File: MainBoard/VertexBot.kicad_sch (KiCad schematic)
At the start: 52 parts, among them J1 Battery, J2 I2C Extension, J4 Left Motor, J5 Right Motor, J6 Led Strip, Q1 BSS138, Q2 BSS138, Q3 BSS138, SW1 SW_SPST, U1 DRV8830DGQR, U10 MAX4466 (LEFT), U11 MAX4466 (RIGHT), U12 ESP32-S3-CAM-B, U13 ESP32-S3-CAM-A, U14 MAX98357A, U2 DRV8830DGQR, U3 S13V30F5, U5 INMP441, U6 0.96 INCH OLED, U7 DRV5033AJxLPG, U8 DRV5033AJxLPG, U9 MPU 6050

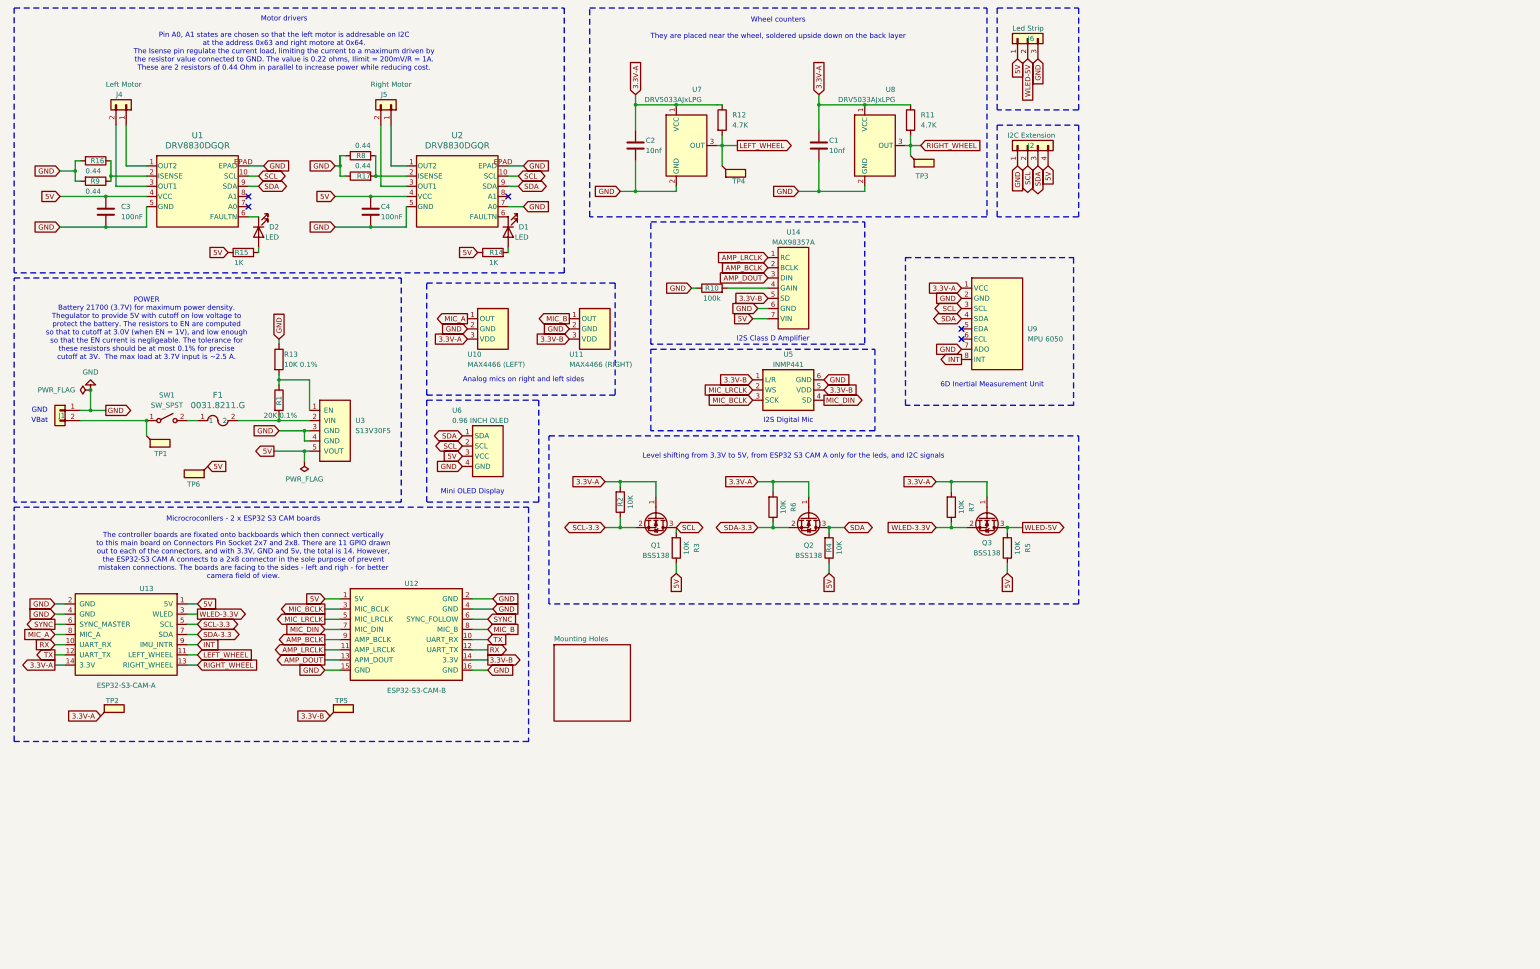
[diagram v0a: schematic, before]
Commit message: Adjust DRV8830DGQR to allow thermal pad connect to GND Adjust some of the modules courtyard Fix mounting holes symbols to have connection
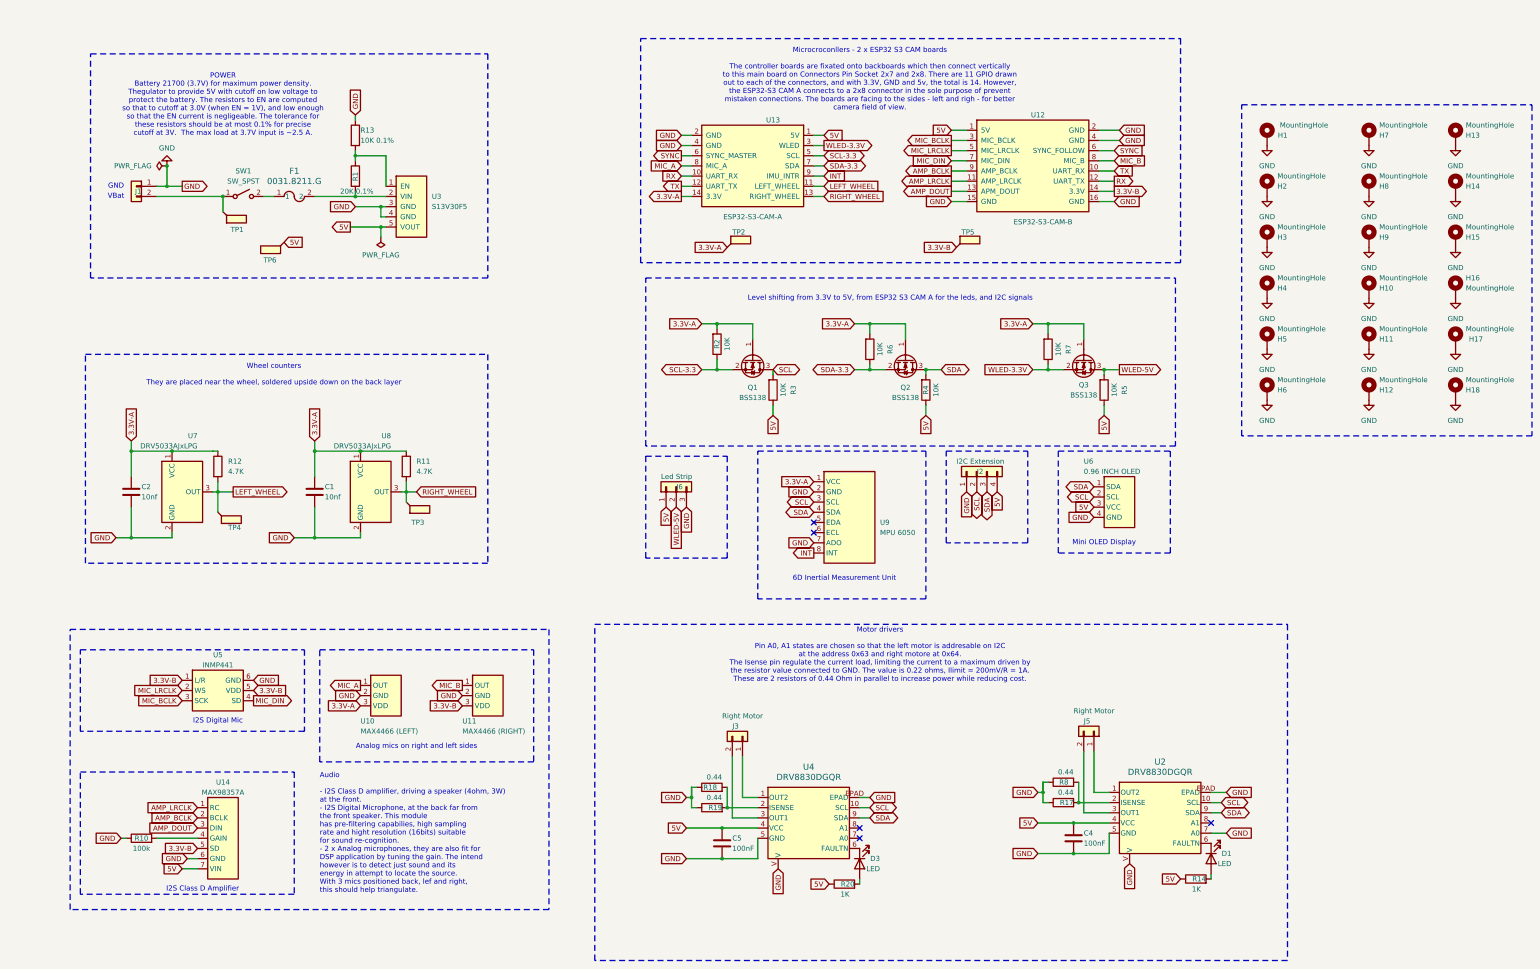
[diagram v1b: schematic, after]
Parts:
- removed C3: 100nF, Capacitor_SMD:C_0603_1608Metric, symbol Device:C
- removed D2: LED, LED_SMD:LED_0805_2012Metric, symbol Device:LED
- removed J4: Left Motor, Connector_JST:JST_PH_S2B-PH-K_1x02_P2.00mm_Horizontal, symbol Connector_Generic:Conn_01x02
- removed R15: 1K, Resistor_SMD:R_0603_1608Metric, symbol Device:R
- removed R16, R9: 0.44, Resistor_SMD:R_0603_1608Metric, symbol Device:R
- removed U1: DRV8830DGQR, Vertex_Bot:DGQ10_2P18X1P72, symbol DRV8830:DRV8830DGQR
- added C5: 100nF, Capacitor_SMD:C_0603_1608Metric, symbol Device:C
- added D3: LED, LED_SMD:LED_0805_2012Metric, symbol Device:LED
- added H1, H10, H11, H12, H13, H14, H15, H16, H17, H18, H2, H3, H4, H5, H6, H7, H8, H9: MountingHole, MountingHole:MountingHole_3.5mm_Pad, symbol Mechanical:MountingHole_Pad
- added J3: Right Motor, Connector_JST:JST_PH_S2B-PH-K_1x02_P2.00mm_Horizontal, symbol Connector_Generic:Conn_01x02
- added R18: 0.44, Resistor_SMD:R_0603_1608Metric, symbol Device:R
- added R19: 0.44, Resistor_SMD:R_1206_3216Metric, symbol Device:R
- added R20: 1K, Resistor_SMD:R_0603_1608Metric, symbol Device:R
- added U4: DRV8830DGQR, Vertex_Bot:DGQ10_2P18X1P72, symbol DRV8830:DRV8830DGQR
- J2: footprint Connector_JST:JST_XH_S3B-XH-A-1_1x03_P2.50mm_Horizontal -> Connector_PinHeader_2.54mm:PinHeader_1x04_P2.54mm_Vertical
- R17: footprint Resistor_SMD:R_0603_1608Metric -> Resistor_SMD:R_1206_3216Metric
- U7, U8: footprint Package_TO_SOT_THT:TO-92Flat -> Package_TO_SOT_THT:TO-92_Inline
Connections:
- net 5V: now also C5.1, R20.1, U4.4 (VCC)
- net GND: now also U2.V, C5.2, H1.1, H10.1, H11.1, H12.1, H13.1, H14.1, H15.1, H16.1, H17.1, H18.1, H2.1, H3.1, H4.1, H5.1, H6.1, H7.1, H8.1, H9.1, R18.1, R19.1, U4.5 (GND), U4.EPAD, U4.V
- net SCL: now also U4.10 (SCL)
- net SDA: now also U4.9 (SDA)
- new net: D3.2 (A), R20.2
- new net: J3.1 (Pin_1), U4.1 (OUT2)
- new net: R18.2, R19.2, U4.2 (ISENSE)
- new net: J3.2 (Pin_2), U4.3 (OUT1)
- new net: D3.1 (K), U4.6 (FAULTN)
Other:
- removed sheet Mounting Holes
- note added: "Audio - I2S Class D amplifier, driving a speaker (4ohm, 3W) at the front. - I2S Digital Microphone, at the back far from the front speaker. This module has pre-filtering capabilies, high sampling rate and hight resolution (16bits) suitable for sound re-cognition. - 2 x Analog microphones, they are also fit for DSP application by tuning the gain. The intend however is to detect just sound and its 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"
- note added: "Level shifting from 3.3V to 5V, from ESP32 S3 CAM A for the leds, and I2C signals"
- note removed: "Level shifting from 3.3V to 5V, from ESP32 S3 CAM A only for the leds, and I2C signals"
- moved on the sheet: C1, C2, C4, D1, F1, J1, J2, J5, J6, Q1, Q2, Q3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

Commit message: Completed Main PCB first draft (v0.1)
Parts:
- removed R18, R8: 0.44, Resistor_SMD:R_0603_1608Metric, symbol Device:R
- C1, C4, C5: footprint Capacitor_SMD:C_0603_1608Metric -> Capacitor_SMD:C_0603_1608Metric_Pad1.08x0.95mm_HandSolder
- D1, D3: footprint LED_SMD:LED_0805_2012Metric -> LED_SMD:LED_0805_2012Metric_Pad1.15x1.40mm_HandSolder
- J1: footprint Connector_JST:JST_XH_S2B-XH-A-1_1x02_P2.50mm_Horizontal -> Connector_BarrelJack:BarrelJack_Kycon_KLDX-0202-xC_Horizontal; symbol Connector_Generic:Conn_01x02 -> Connector:Barrel_Jack_Switch; Buy (none) -> https://au.element14.com/kycon/kldx-0202-a/dc-power-jack-2m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
- J3: renamed from J5; value Right Motor -> Left Motor
- J6: footprint Connector_JST:JST_XH_S3B-XH-A-1_1x03_P2.50mm_Horizontal -> Connector_JST:JST_PH_B3B-PH-K_1x03_P2.00mm_Vertical
- R1, R10, R11, R12, R13, R14, R2, R20, R3, R4, R5, R6, R7: footprint Resistor_SMD:R_0603_1608Metric -> Resistor_SMD:R_0603_1608Metric_Pad0.98x0.95mm_HandSolder
- R17, R19: value 0.44 -> 0.22; footprint Resistor_SMD:R_1206_3216Metric -> Resistor_SMD:R_2512_6332Metric_Pad1.40x3.35mm_HandSolder
- U10, U11: footprint Connector_PinSocket_2.54mm:PinSocket_1x03_P2.54mm_Vertical -> Vertex_Bot:MAX4466_VERTICAL
- U3: footprint Vertex_Bot:S13V30F5_VERTICAL -> Vertex_Bot:S13V30F5_HORIZONTAL
- U7, U8: footprint Package_TO_SOT_THT:TO-92_Inline -> Package_TO_SOT_THT:TO-92Flat
- renumbered J3 to J5
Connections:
- net Vbat: now reaches J1.2, SW1.1 (A), TP1.1
- net Vbat: now also J1.3
- net Vin: now reaches F1.2, R1.2, U3.2 (VIN)
- net SWITCH: now reaches F1.1, SW1.2 (B)
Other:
- note removed: "GND"
- note removed: "VBat"

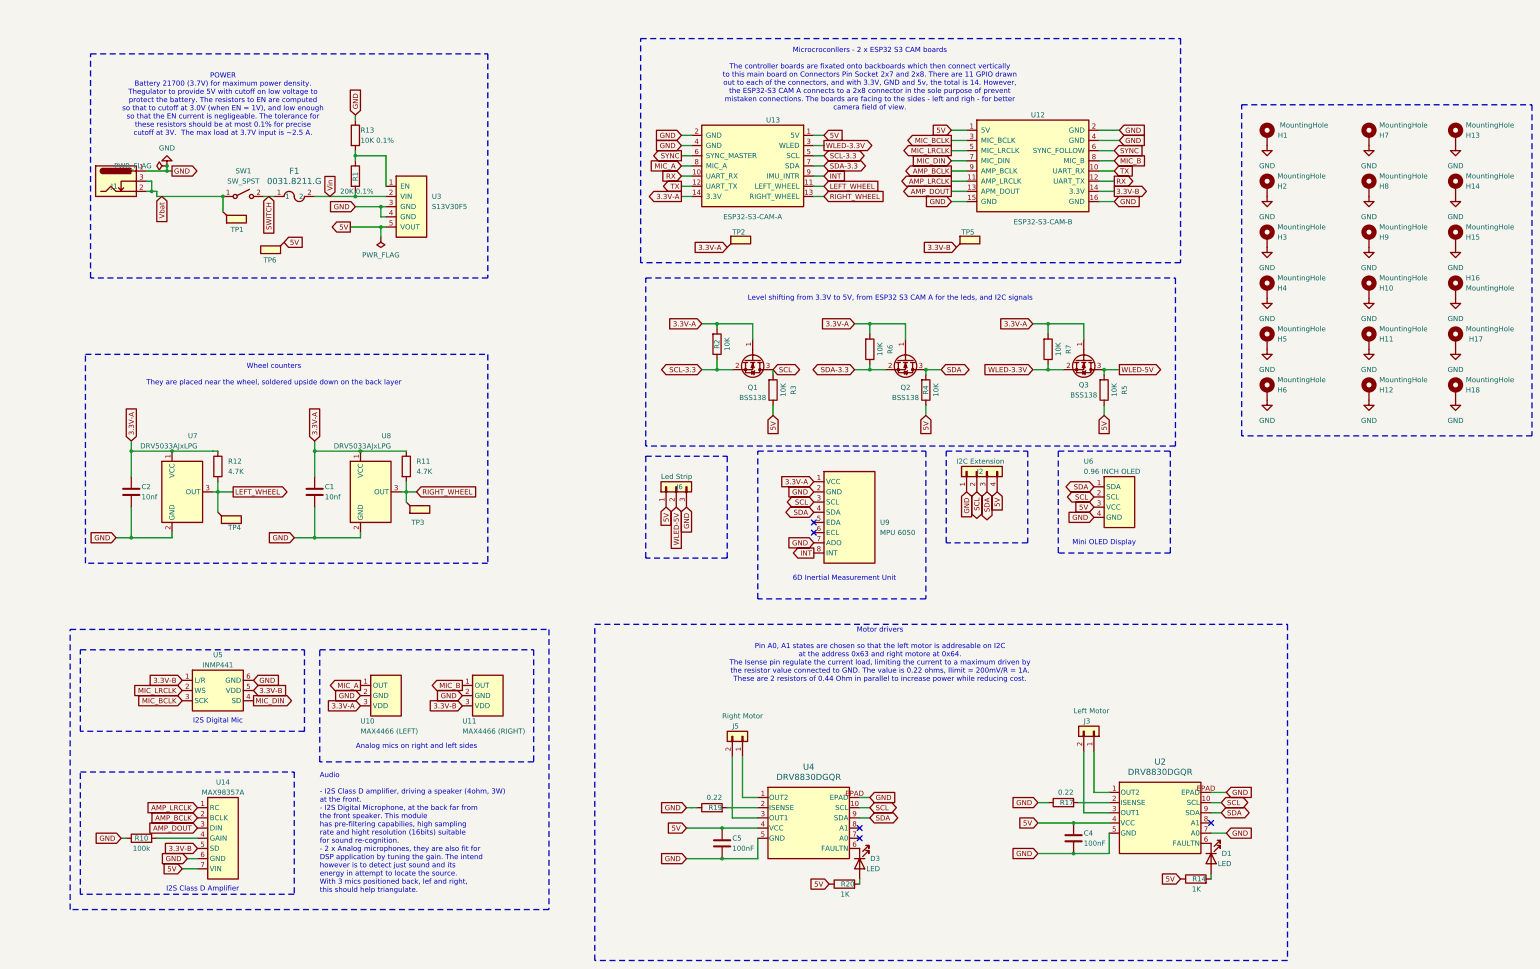
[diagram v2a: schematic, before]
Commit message: Reviewed power requirements, adjusted power track widths Changed to DC barel connector with proper current rating Added corresponding symbol, footprint and 3D model
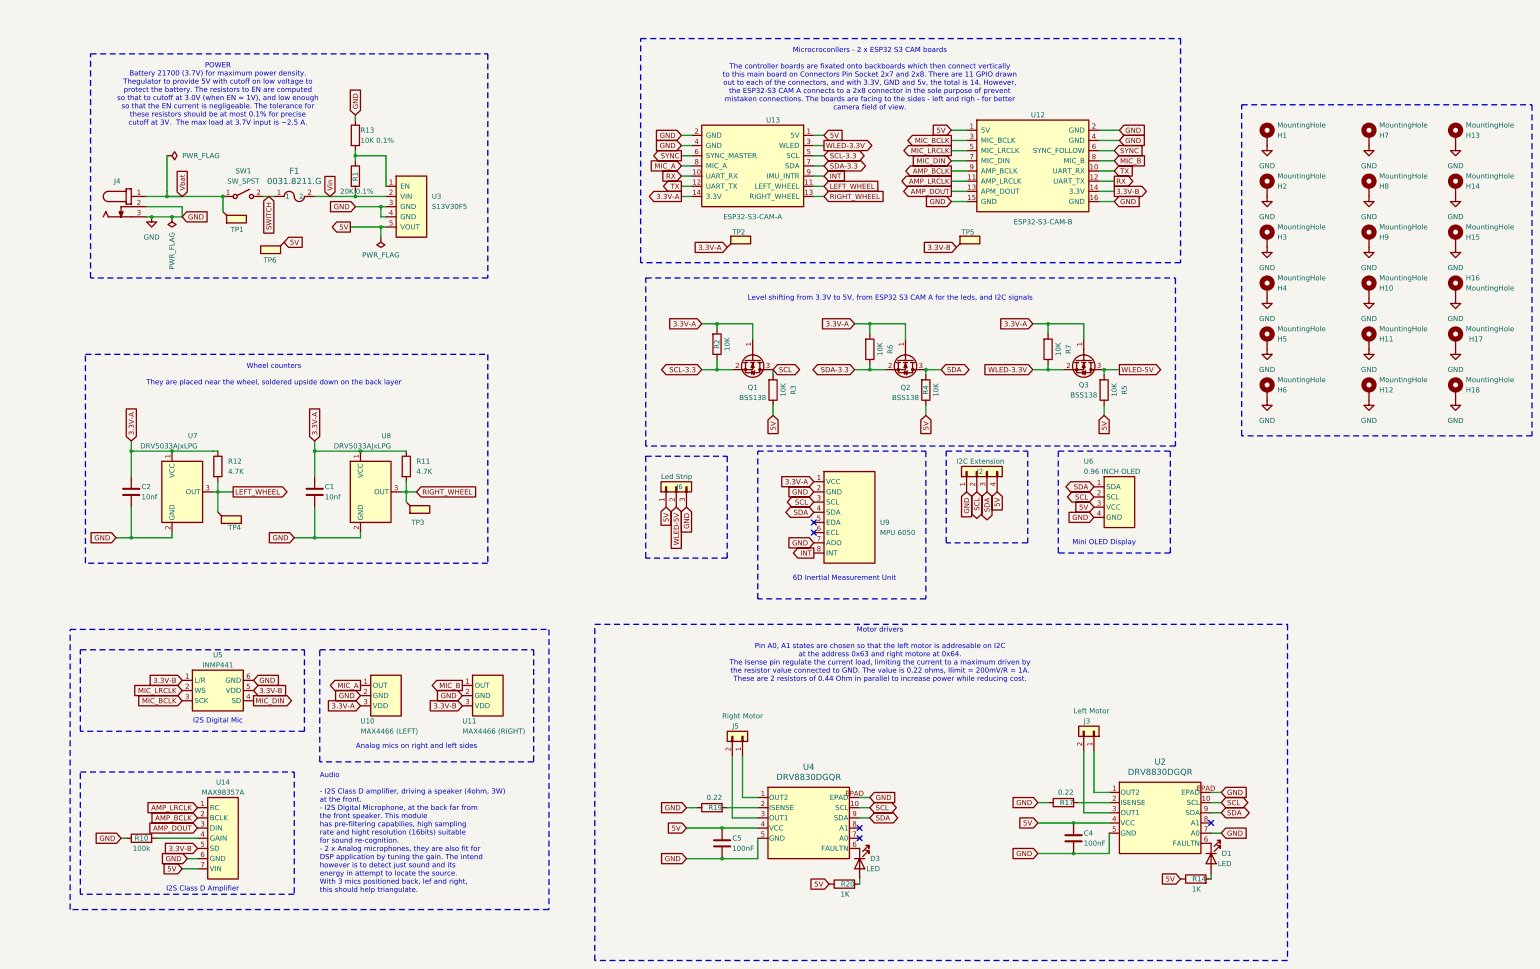
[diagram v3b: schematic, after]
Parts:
- removed J1: Battery, Connector_BarrelJack:BarrelJack_Kycon_KLDX-0202-xC_Horizontal, symbol Connector:Barrel_Jack_Switch
- added J4: 694106301002, Connector_THT_Wurth:J_Wurth_WR-DC_694106301002, symbol Connector_Wurth_WR-DC:694106301002
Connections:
- net GND: now also J4.2, J4.3
- net Vbat: now also J4.1

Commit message: Move MAX4466 (analog mics) away from USP connectors All 3D models update Add silkscreen user labels
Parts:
- U10, U11: footprint Vertex_Bot:MAX4466_VERTICAL -> Vertex_Bot:MAX4466_HORIZONTAL
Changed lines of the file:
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@@
 			)
 		)
-		(property "Footprint" "Vertex_Bot:MAX4466_VERTICAL"
+		(property "Footprint" "Vertex_Bot:MAX4466_HORIZONTAL"
 			(at 106.68 180.34 0)
 			(effects
@@
 			)
 		)
-		(property "Footprint" "Vertex_Bot:MAX4466_VERTICAL"
+		(property "Footprint" "Vertex_Bot:MAX4466_HORIZONTAL"
 			(at 132.08 180.34 0)
 			(effects
@@
 			)
 		)
-		(property "Description" ""
+		(property "Description" "https://www.digikey.com/en/products/detail/schurter-inc/0031-8211/669926"
 			(at 82.55 60.96 0)
 			(effects
@@
 			)
 		)
-		(property "Datasheet" "~"
+		(property "Datasheet" "https://www.digikey.com/en/products/detail/c-k/L101011MS02Q/484142"
 			(at 74.93 60.96 0)
 			(effects

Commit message: All project library paths relative to project folder
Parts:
- F1, J2, J3, J4, J5, J6, SW1, U10, U11, U12, U13, U14, U3, U5, U6, U9: now left out of the parts list

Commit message: JLCPCB parts, refs, shops Corrected missing pins for backboard B
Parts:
- C1, C2: value 10nf -> 100nf; LCSC Part # (none) -> C343025
- C4, C5: LCSC Part # (none) -> C343025
- D1, D3: LCSC Part # (none) -> C264416
- F1: Price (none) -> $2.53; Shop (none) -> digikey.com.au (ref 0031.8201.G)
- J2: Price (none) -> $0.48
- J3: Price (none) -> $1.17; Shop (none) -> digikey.com.au
- J4: Price (none) -> $1.41; Shop https://au.element14.com/wurth-elektronik/694106301002/conn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 -> digikey.com.au (ref 694106301002)
- J5: Price (none) -> $1.17; Shop (none) -> digikey.com.au (ref S2B-PH-K-S)
- J6: Price (none) -> $0.23; Shop (none) -> digikey.com.au (ref B3B-PH-K-S)
- R10: LCSC Part # (none) -> C15458
- R11, R12: LCSC Part # (none) -> C2784998
- R13: LCSC Part # (none) -> C413738
- R14, R20: LCSC Part # (none) -> C2774267
- R17, R19: LCSC Part # (none) -> C49655446
- R2, R3, R4, R5, R6, R7: LCSC Part # (none) -> C15401
- SW1: Price (none) -> $6.13; Shop (none) -> L101011MS02Q (ref L101011MS02Q)
- U10, U11: Price (none) -> $1.99; Shop (none) -> (3 pins) https://www.aliexpress.com/item/1005012568399288.h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
- U12: Price (none) -> $2.05 (5 for $11); Shop (none) -> (PCBWAY)
- U13: Price (none) -> $2.05; Shop (none) -> (PCBWAY)
- U14: Price (none) -> $3.04; Shop (none) -> https://www.aliexpress.com/item/1005006096022361.html
- U2, U4: LCSC Part # (none) -> C127591
- U3: Price (none) -> $30; Shop (none) -> Core Electronics
- U5: Price (none) -> $3; Shop (none) -> https://www.aliexpress.com/item/1005013251461379.html
- U6: Price (none) -> $3.85; Shop (none) -> :https://www.aliexpress.com/item/1005006901360788.html (SSD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
- U7, U8: LCSC Part # (none) -> C201608
- U9: Price (none) -> $4.29; Shop (none) -> https://www.aliexpress.com/item/1005008714169630.html
